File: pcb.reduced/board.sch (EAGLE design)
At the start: 24 parts, among them Q1 MPSA42

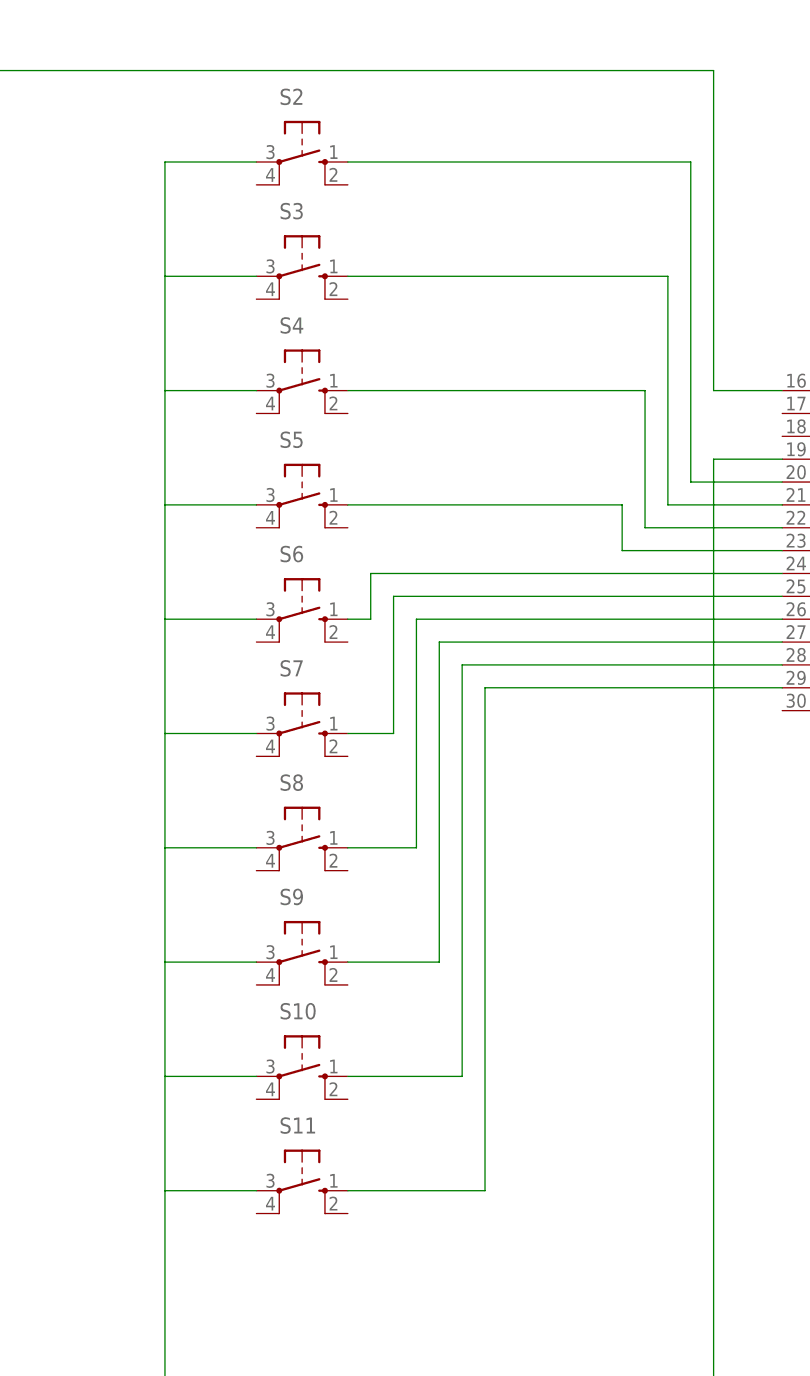
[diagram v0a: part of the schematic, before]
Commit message: Use bigger buttons and re-layout.
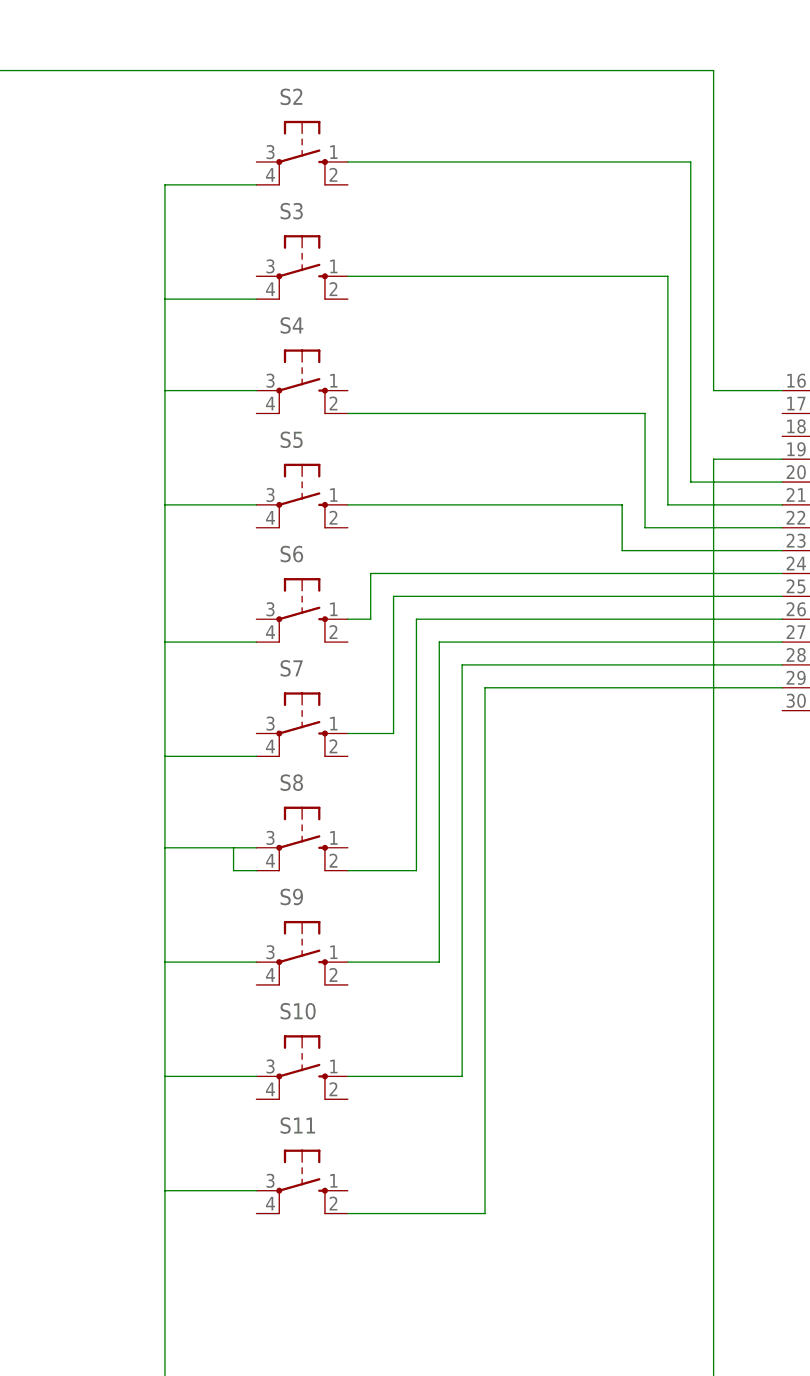
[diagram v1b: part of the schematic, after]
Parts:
- S10, S11, S2, S3, S4, S5, S6, S7, S8, S9: device switch-omron:10-XX -> switch-omron:40-XX
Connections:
- net GND: now also S2.P1, S3.P1, S6.P1, S7.P1, S8.P1; no longer S2.P, S3.P, S6.P, S7.P
- net N$12: now also S11.S1; no longer S11.S
- net N$5: now also S4.S1; no longer S4.S
- net N$9: now also S8.S1; no longer S8.S
